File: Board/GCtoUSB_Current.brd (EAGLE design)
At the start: 38.1 x 61 mm, 40 parts, among them J1 AVR_SPI_PRG_6PTH, J2 AVR_SPI_PRG_6PTH, U1 ATMEGA8U2AU, U2 3.3V_REG_LDOSMD, X1 USB-MB-H, Y1 16MHz, Y2 16MHz

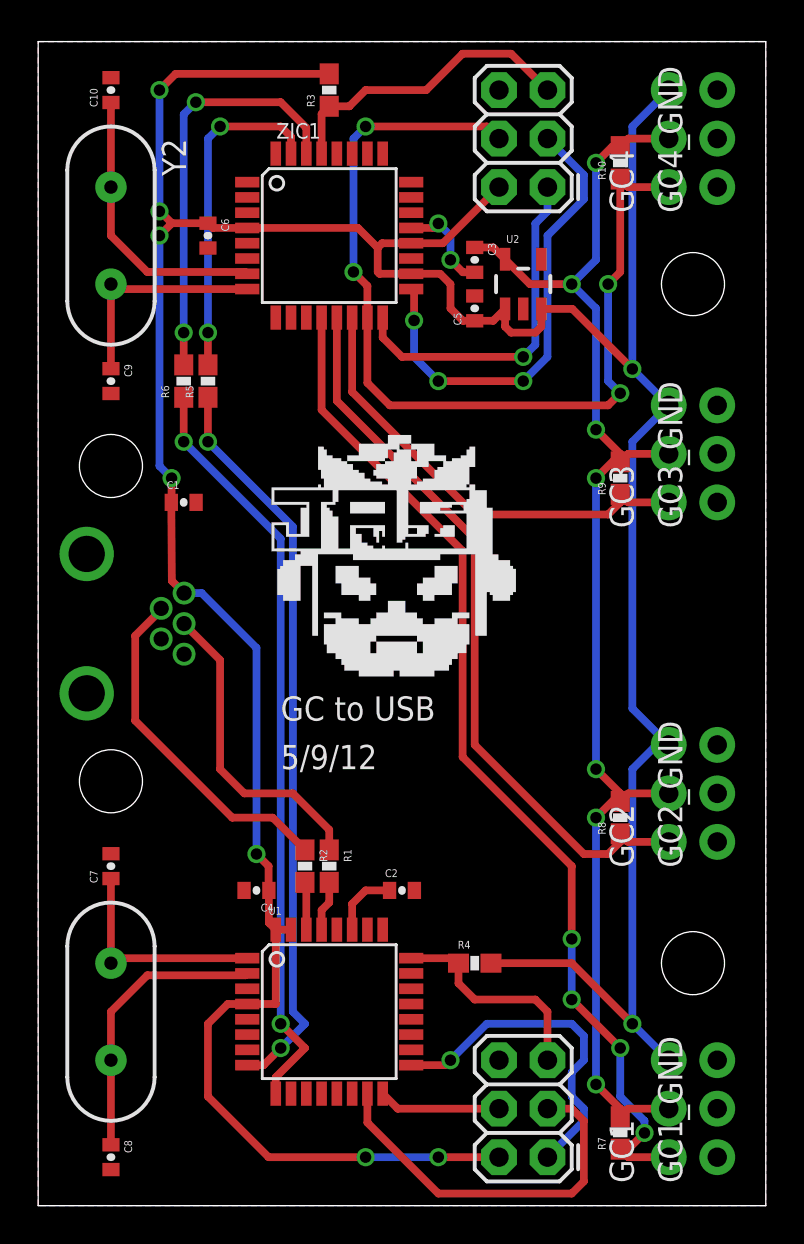
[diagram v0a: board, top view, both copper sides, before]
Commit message: Moved to eagle 6.2. Completed SMT version of board - now saved as version 1.3.
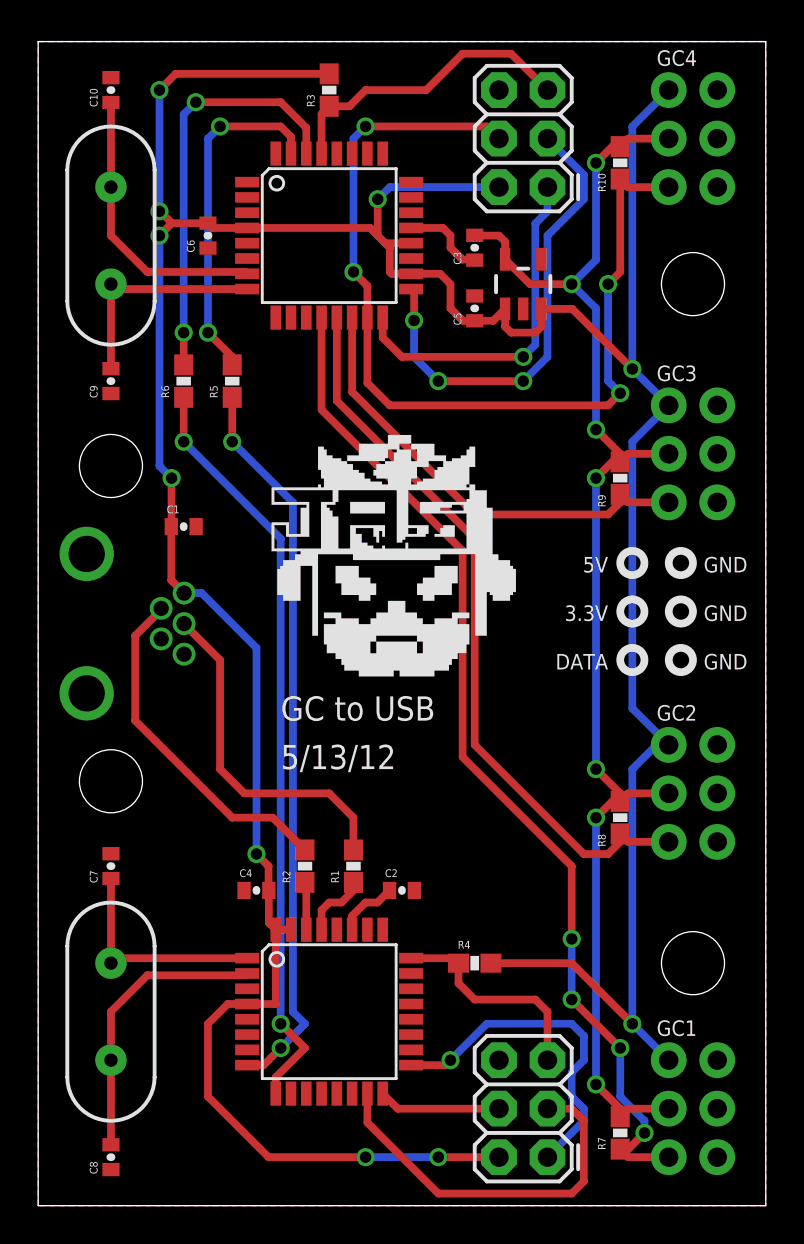
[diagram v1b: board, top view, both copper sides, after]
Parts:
- U1: value ATMEGA8U2AU -> 8U2
- ZIC1: value ATMEGA328 -> 328
- moved R1 1.27 mm to (16.5, 17.8)
- moved R5 1.27 mm to (10.2, 43.2)
- moved C1 1.27 mm to (7.62, 35.6)
- moved C3 0.63 mm to (22.9, 50.2)
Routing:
- net 5V: track 189.5 -> 191.8 mm, vias 9 -> 10
- net N$5: track 16.5 -> 18.1 mm
- net N$3: track 2.64 -> 3.54 mm
- net GND: track 5.23 -> 4.41 mm, vias 2 -> 0
- net 3.3V: track 72.8 -> 73.6 mm
- net TX_328: track 17.6 -> 18.1 mm
- net RX_8U2: track 38.8 -> 38.3 mm
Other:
- board text added: "3.3V"
- board text added: "5/13/12"
- board text added: "5V"
- board text added: "DATA"
- board text added: "GND"
- board text removed: "5/9/12"
